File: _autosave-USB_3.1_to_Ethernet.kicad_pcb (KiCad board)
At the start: 4 copper layers, 75 x 25 mm, 10 parts, among them J1 RJ45_JK0654219, J2 USB3_A, U1 LAN7801_9JX, U2 93LC56B_SN, U3 KSZ9031RNXCC, U4 TLV76733QWDRBxQ1, U5 USBLC6-2P6, U6 TPS7A0230PDQNR, Y1 C3E-8.000-18-3030-R

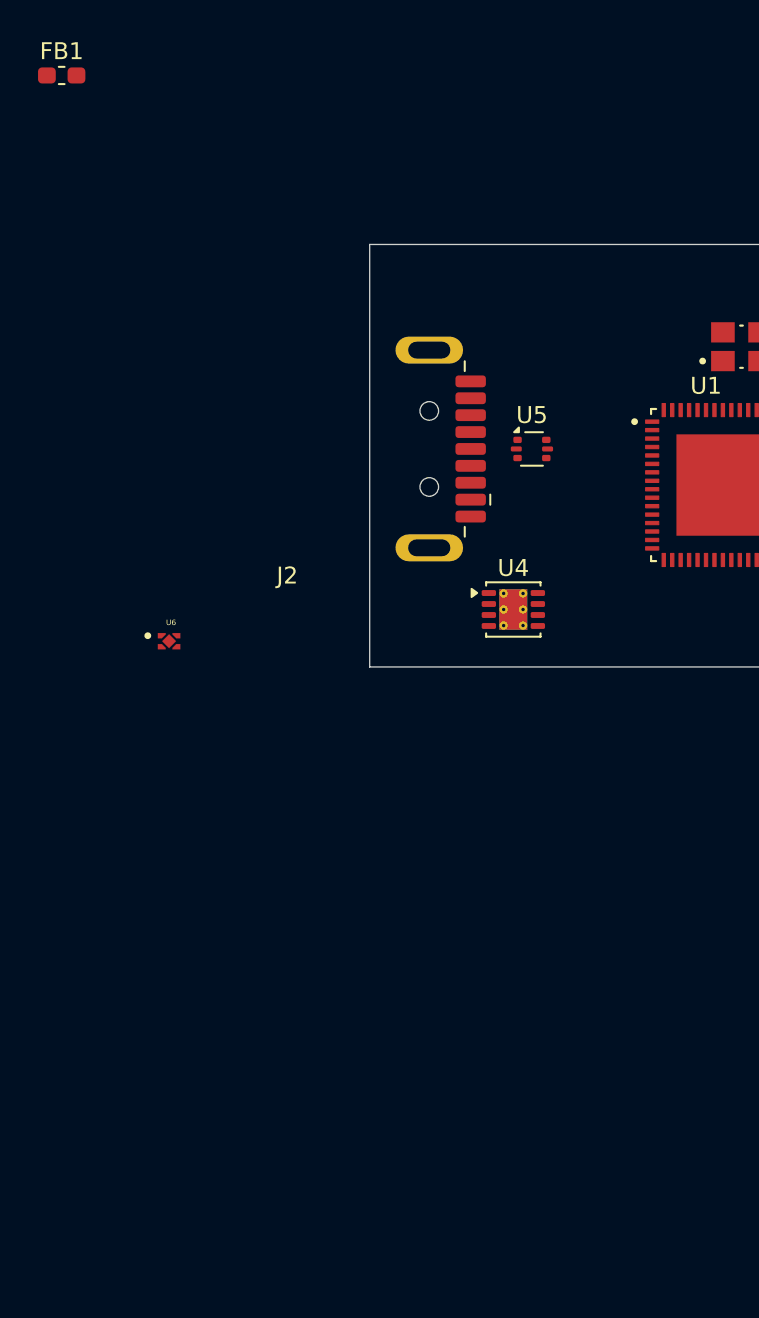
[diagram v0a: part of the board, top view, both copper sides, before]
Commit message: power section added and power connections made
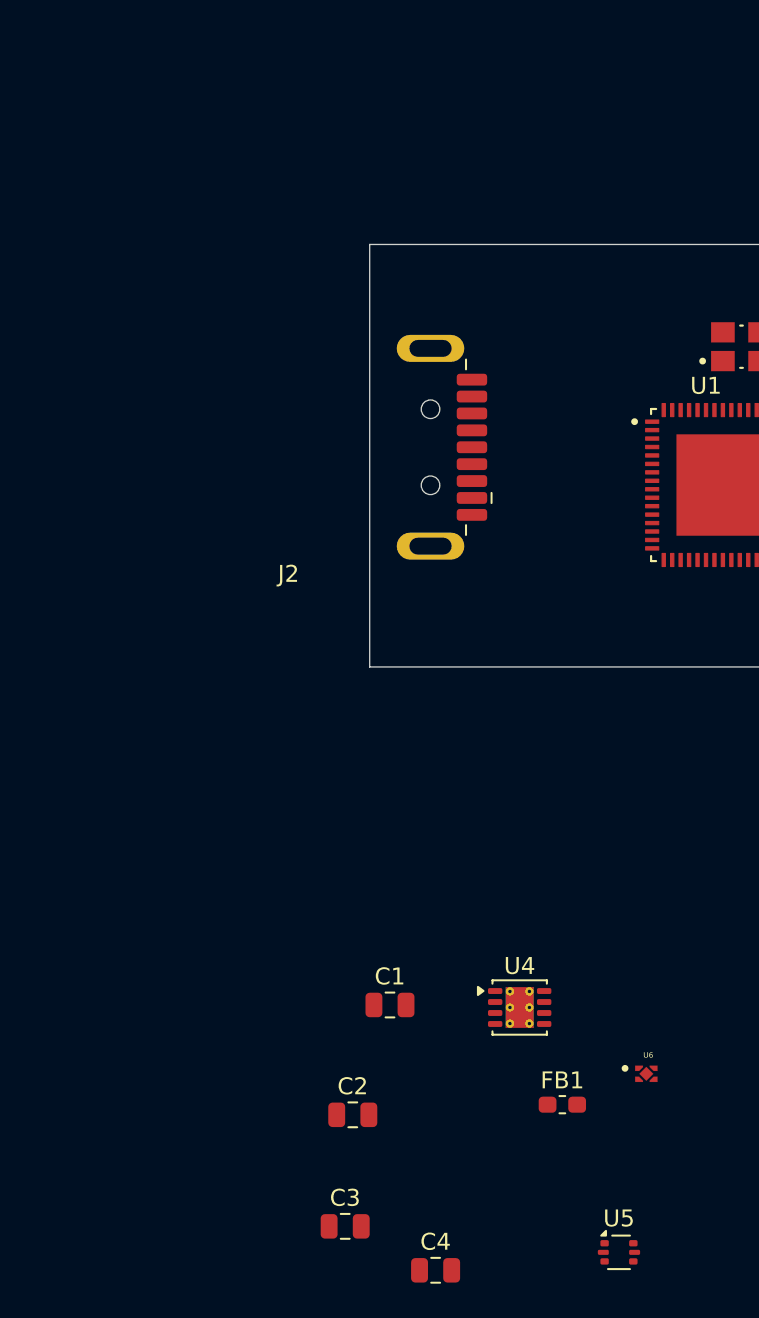
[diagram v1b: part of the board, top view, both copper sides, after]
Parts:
- added C1: 1uF, Capacitor_SMD:C_0805_2012Metric, F.Cu at (60.9, 95.1)
- added C2: 1uF, Capacitor_SMD:C_0805_2012Metric, F.Cu at (58.7, 101.6)
- added C3: 1uF, Capacitor_SMD:C_0805_2012Metric, F.Cu at (58.2, 108.2)
- added C4: 1uF, Capacitor_SMD:C_0805_2012Metric, F.Cu at (63.6, 110.8)
- U4: value TLV76733QWDRBxQ1 -> TLV76733
- U6: value TPS7A0230PDQNR -> TPS7A0212
- moved FB1 67.7 mm to (71.1, 101.0)
- moved U5 47.8 mm to (74.5, 109.7)
- moved U6 38.1 mm to (76.1, 99.2)
- moved U4 23.6 mm to (68.6, 95.2)
- moved J2 0.12 mm to (54.9, 62.1)
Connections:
- FB1 pad 1: unconnected-(FB1-Pad1) -> VBUS
- FB1 pad 2: unconnected-(FB1-Pad2) -> +5V
- J2 pad 1: unconnected-(J2-VBUS-Pad1) -> VBUS
- J2 pad 10: unconnected-(J2-SHIELD-Pad10) -> GND
- J2 pad 2: unconnected-(J2-D--Pad2) -> Net-(J2-D-)
- J2 pad 3: unconnected-(J2-D+-Pad3) -> Net-(J2-D+)
- J2 pad 4: unconnected-(J2-GND-Pad4) -> GND
- J2 pad 5: unconnected-(J2-SSRX--Pad5) -> SSRX-
- J2 pad 6: unconnected-(J2-SSRX+-Pad6) -> SSRX+
- J2 pad 7: unconnected-(J2-DRAIN-Pad7) -> GND
- J2 pad 8: unconnected-(J2-SSTX--Pad8) -> SSTX-
- J2 pad 9: unconnected-(J2-SSTX+-Pad9) -> SSTX+
- U4 pad 1: unconnected-(U4-OUT-Pad1) -> 3v3_out
- U4 pad 3: unconnected-(U4-SNS-Pad3) -> 3v3_out
- U4 pad 4: Net-(U4-GND-Pad4) -> GND
- U4 pad 5: unconnected-(U4-EN-Pad5) -> +5V
- U4 pad 6: Net-(U4-GND-Pad4) -> GND
- U4 pad 8: unconnected-(U4-IN-Pad8) -> +5V
- U4 pad 9: unconnected-(U4-PAD-Pad9) -> GND
- U5 pad 1: unconnected-(U5-I/O1-Pad1) -> Net-(J2-D-)
- U5 pad 2: unconnected-(U5-GND-Pad2) -> GND
- U5 pad 3: unconnected-(U5-I/O2-Pad3) -> Net-(J2-D+)
- U5 pad 4: unconnected-(U5-I/O2-Pad4) -> D+
- U5 pad 5: unconnected-(U5-VBUS-Pad5) -> +5V
- U5 pad 6: unconnected-(U5-I/O1-Pad6) -> D-
- U6 pad 1: unconnected-(U6-OUT-Pad1) -> 1v2_core
- U6 pad 2: unconnected-(U6-GND-Pad2) -> GND
- U6 pad 3: unconnected-(U6-EN-Pad3) -> +5V
- U6 pad 4: unconnected-(U6-IN-Pad4) -> +5V
- U6 pad 5: unconnected-(U6-THERMAL_PAD-Pad5) -> GND
